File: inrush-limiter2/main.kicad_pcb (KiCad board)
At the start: 2 copper layers, 33 parts, among them K1 RELAY_2RT, P1 CONN_01X04, P2 CONN_01X02, Q1 2N3904, Q2 PN2222A, T1 MY-TRANSFO, U1 LM393, U2 50 ohm NTC

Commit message: good
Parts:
- moved D6 2.54 mm to (148.6, 87.6)
- moved P2 2.54 mm to (143.5, 92.7)
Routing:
- net Net-(D6-Pad1): track 49.8 -> 47.1 mm
- net Net-(D6-Pad2): track 3.81 -> 5.61 mm
- net GND: track 242.2 -> 243.7 mm
- net +5V: track 120.7 -> 119.2 mm
- added copper zone on B.Cu, net GND
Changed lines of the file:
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@@
     (links 59)
     (no_connects 0)
-    (area 110.105 47.685 234.358001 96.28099)
+    (area 110.105 47.685 234.358001 100.585)
     (thickness 1.6)
     (drawings 0)
-    (tracks 192)
+    (tracks 187)
     (zones 0)
     (modules 33)
@@
   )
   (module LEDs:LED-5MM (layer F.Cu)
-    (at 146.05 87.63 90)
+    (at 148.59 87.63 90)
     (descr "LED 5mm round vertical")
     (tags "LED 5mm round vertical")
@@
   )
   (module Pin_Headers:Pin_Header_Straight_1x02 (layer F.Cu)
-    (at 140.97 92.71 180)
+    (at 143.51 92.71 180)
     (descr "Through hole pin header")
     (tags "pin header")
@@
   (segment (start 142.24202 69.85) (end 142.24254 69.85052) (width 1) (layer B.Cu) (net 1) (status 30))
   (segment (start 138.43 69.84798) (end 138.43254 69.85052) (width 1) (layer B.Cu) (net 1) (status 30))
-  (segment (start 137.16 95.25) (end 139.7 95.25) (width 1) (layer B.Cu) (net 2))
-  (segment (start 140.97 93.98) (end 140.97 92.71) (width 1) (layer B.Cu) (net 2) (status 20))
   (segment (start 139.7 95.25) (end 140.97 93.98) (width 1) (layer B.Cu) (net 2))
+  (segment (start 140.97 93.98) (end 143.51 92.71) (width 1) (layer B.Cu) (net 2) (status 20))
+  (segment (start 139.7 95.25) (end 137.16 95.25) (width 1) (layer B.Cu) (net 2))
   (segment (start 149.85746 69.84948) (end 149.85746 74.92746) (width 1) (layer B.Cu) (net 2) (status 10))
   (segment (start 160.02 50.8) (end 146.05 50.8) (width 1) (layer B.Cu) (net 2))
@@
   (segment (start 185.42 59.69) (end 178.74996 59.69) (width 0.75) (layer B.Cu) (net 11) (status 10))
   (segment (start 178.74996 59.69) (end 177.63998 58.58002) (width 0.75) (layer B.Cu) (net 11) (status 20))
-  (segment (start 146.05 81.28) (end 146.05 85.09) (width 1) (layer B.Cu) (net 12) (status 30))
+  (segment (start 146.05 81.28) (end 147.32 81.28) (width 1) (layer B.Cu) (net 12) (status 10))
+  (segment (start 148.59 82.55) (end 148.59 85.09) (width 1) (layer B.Cu) (net 12) (status 20))
+  (segment (start 147.32 81.28) (end 148.59 82.55) (width 1) (layer B.Cu) (net 12))
   (segment (start 130.81 54.61) (end 130.81 57.15) (width 1) (layer B.Cu) (net 13) (status 10))
   (segment (start 128.27 59.69) (end 127 59.69) (width 1) (layer B.Cu) (net 13) (status 20))
@@
   (segment (start 138.43 59.69306) (end 138.43254 59.69052) (width 1) (layer B.Cu) (net 15) (status 30))
   (segment (start 149.85642 59.69052) (end 149.85746 59.68948) (width 1) (layer B.Cu) (net 15) (status 30))
-  (segment (start 146.05 87.63) (end 143.51 87.63) (width 1) (layer B.Cu) (net 16) (status 400000))
-  (segment (start 143.51 87.63) (end 140.97 85.09) (width 1) (layer B.Cu) (net 16) (status 800000))
-  (segment (start 146.05 87.63) (end 146.05 90.17) (width 1) (layer B.Cu) (net 16) (status 400000))
-  (segment (start 149.86 91.44) (end 185.42 91.44) (width 1) (layer B.Cu) (net 16) (status 10))
-  (segment (start 147.32 91.44) (end 149.86 91.44) (width 1) (layer B.Cu) (net 16))
-  (segment (start 146.05 90.17) (end 147.32 91.44) (width 1) (layer B.Cu) (net 16))
-  (segment (start 140.97 85.09) (end 142.24 85.09) (width 1) (layer B.Cu) (net 16) (status 10))
+  (segment (start 148.59 87.63) (end 147.32 87.63) (width 1) (layer B.Cu) (net 16) (status 10))
+  (segment (start 144.78 85.09) (end 140.97 85.09) (width 1) (layer B.Cu) (net 16) (status 20))
+  (segment (start 147.32 87.63) (end 144.78 85.09) (width 1) (layer B.Cu) (net 16))
+  (segment (start 148.59 87.63) (end 152.4 91.44) (width 1) (layer B.Cu) (net 16) (status 10))
+  (segment (start 152.4 91.44) (end 185.42 91.44) (width 1) (layer B.Cu) (net 16) (status 20))
   (segment (start 185.42 66.04) (end 185.42 71.12) (width 1) (layer B.Cu) (net 17) (status 30))
   (segment (start 185.42 71.12) (end 185.42 76.2) (width 1) (layer B.Cu) (net 17) (status 30))
@@
   (segment (start 119.38 77.47) (end 118.11 77.47) (width 1) (layer B.Cu) (net 21) (status 20))
   (segment (start 120.65 76.2) (end 119.38 77.47) (width 1) (layer B.Cu) (net 21))
-  (segment (start 139.7 81.28) (end 138.43 81.28) (width 1) (layer B.Cu) (net 22))
+  (segment (start 144.78 90.17) (end 148.59 93.98) (width 1) (layer B.Cu) (net 22))
+  (segment (start 137.16 83.82) (end 143.51 90.17) (width 1) (layer B.Cu) (net 22) (status 30))
+  (segment (start 143.51 90.17) (end 144.78 90.17) (width 1) (layer B.Cu) (net 22) (status 10))
+  (segment (start 190.5 93.98) (end 148.59 93.98) (width 1) (layer B.Cu) (net 22))
+  (segment (start 193.04 91.44) (end 190.5 93.98) (width 1) (layer B.Cu) (net 22) (status 10))
+  (segment (start 140.97 81.28) (end 138.43 81.28) (width 1) (layer B.Cu) (net 22))
   (segment (start 142.24 73.66) (end 143.51 74.93) (width 1) (layer B.Cu) (net 22))
   (segment (start 143.51 74.93) (end 143.51 78.74) (width 1) (layer B.Cu) (net 22))
   (segment (start 143.51 78.74) (end 140.97 81.28) (width 1) (layer B.Cu) (net 22))
-  (segment (start 140.97 81.28) (end 139.7 81.28) (width 1) (layer B.Cu) (net 22))
-  (segment (start 137.16 82.55) (end 137.16 83.82) (width 1) (layer B.Cu) (net 22) (status 800000))
+  (segment (start 137.16 82.55) (end 137.16 83.82) (width 1) (layer B.Cu) (net 22) (status 20))
   (segment (start 138.43 81.28) (end 137.16 82.55) (width 1) (layer B.Cu) (net 22))
-  (segment (start 146.05 93.98) (end 144.78 92.71) (width 1) (layer B.Cu) (net 22))
-  (segment (start 142.24 90.17) (end 143.51 91.44) (width 1) (layer B.Cu) (net 22))
-  (segment (start 143.51 91.44) (end 144.78 92.71) (width 1) (layer B.Cu) (net 22))
-  (segment (start 142.24 90.17) (end 140.97 90.17) (width 1) (layer B.Cu) (net 22) (status 10))
-  (segment (start 190.5 93.98) (end 146.05 93.98) (width 1) (layer B.Cu) (net 22))
-  (segment (start 193.04 91.44) (end 190.5 93.98) (width 1) (layer B.Cu) (net 22) (status 10))
-  (segment (start 140.97 90.17) (end 139.7 88.9) (width 1) (layer B.Cu) (net 22) (status 10))
-  (segment (start 139.7 86.36) (end 137.16 83.82) (width 1) (layer B.Cu) (net 22) (status 20))
-  (segment (start 139.7 86.36) (end 139.7 88.9) (width 1) (layer B.Cu) (net 22))
   (segment (start 146.05 73.66) (end 142.24 73.66) (width 1) (layer B.Cu) (net 22) (status 10))
   (segment (start 138.43 73.66) (end 142.24 73.66) (width 1) (layer B.Cu) (net 22) (status 10))
@@
   (segment (start 137.16 78.74) (end 139.7 78.74) (width 1) (layer B.Cu) (net 24) (status 10))
   (segment (start 139.7 78.74) (end 140.97 77.47) (width 1) (layer B.Cu) (net 24) (status 20))
+  (zone (net 2) (net_name GND) (layer B.Cu) (hatch edge 0.508)
+    (connect_pads (clearance 0.508))
+    (min_thickness 0.254)
+    (fill yes (arc_segments 16) (thermal_gap 0.508) (thermal_bridge_width 0.508))
+    (polygon
+      (pts
+        (xy 167.64 95.25) (xy 114.3 95.25) (xy 114.3 50.8) (xy 167.64 50.8) (xy 167.64 95.25)
+      )
+    )
+  )
 )

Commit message: more tidying
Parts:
- moved D6 4.02 mm to (149.9, 91.4)
- moved P2 1.80 mm to (142.2, 91.4)
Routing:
- net Net-(D6-Pad2): track 5.61 -> 9.54 mm
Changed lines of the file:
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@@
     (links 59)
     (no_connects 0)
-    (area 110.105 47.685 234.358001 100.585)
+    (area 110.105 47.685 234.358001 99.315)
     (thickness 1.6)
     (drawings 0)
-    (tracks 187)
+    (tracks 188)
     (zones 0)
     (modules 33)
@@
   )
   (module LEDs:LED-5MM (layer F.Cu)
-    (at 148.59 87.63 90)
+    (at 149.86 91.44 90)
     (descr "LED 5mm round vertical")
     (tags "LED 5mm round vertical")
@@
   )
   (module Pin_Headers:Pin_Header_Straight_1x02 (layer F.Cu)
-    (at 143.51 92.71 180)
+    (at 142.24 91.44 180)
     (descr "Through hole pin header")
     (tags "pin header")
@@
   (segment (start 138.43 69.84798) (end 138.43254 69.85052) (width 1) (layer B.Cu) (net 1) (status 30))
   (segment (start 139.7 95.25) (end 140.97 93.98) (width 1) (layer B.Cu) (net 2))
-  (segment (start 140.97 93.98) (end 143.51 92.71) (width 1) (layer B.Cu) (net 2) (status 20))
+  (segment (start 140.97 93.98) (end 142.24 91.44) (width 1) (layer B.Cu) (net 2) (status 20))
   (segment (start 139.7 95.25) (end 137.16 95.25) (width 1) (layer B.Cu) (net 2))
   (segment (start 149.85746 69.84948) (end 149.85746 74.92746) (width 1) (layer B.Cu) (net 2) (status 10))
@@
   (segment (start 178.74996 59.69) (end 177.63998 58.58002) (width 0.75) (layer B.Cu) (net 11) (status 20))
   (segment (start 146.05 81.28) (end 147.32 81.28) (width 1) (layer B.Cu) (net 12) (status 10))
-  (segment (start 148.59 82.55) (end 148.59 85.09) (width 1) (layer B.Cu) (net 12) (status 20))
+  (segment (start 148.59 82.55) (end 149.86 88.9) (width 1) (layer B.Cu) (net 12) (status 20))
   (segment (start 147.32 81.28) (end 148.59 82.55) (width 1) (layer B.Cu) (net 12))
   (segment (start 130.81 54.61) (end 130.81 57.15) (width 1) (layer B.Cu) (net 13) (status 10))
@@
   (segment (start 138.43 59.69306) (end 138.43254 59.69052) (width 1) (layer B.Cu) (net 15) (status 30))
   (segment (start 149.85642 59.69052) (end 149.85746 59.68948) (width 1) (layer B.Cu) (net 15) (status 30))
-  (segment (start 148.59 87.63) (end 147.32 87.63) (width 1) (layer B.Cu) (net 16) (status 10))
-  (segment (start 144.78 85.09) (end 140.97 85.09) (width 1) (layer B.Cu) (net 16) (status 20))
-  (segment (start 147.32 87.63) (end 144.78 85.09) (width 1) (layer B.Cu) (net 16))
-  (segment (start 148.59 87.63) (end 152.4 91.44) (width 1) (layer B.Cu) (net 16) (status 10))
-  (segment (start 152.4 91.44) (end 185.42 91.44) (width 1) (layer B.Cu) (net 16) (status 20))
+  (segment (start 143.51 85.09) (end 140.97 85.09) (width 1) (layer B.Cu) (net 16))
+  (segment (start 149.86 91.44) (end 143.51 85.09) (width 1) (layer B.Cu) (net 16))
+  (segment (start 149.86 91.44) (end 149.86 91.44) (width 1) (layer B.Cu) (net 16) (status 10))
+  (segment (start 149.86 91.44) (end 149.86 91.44) (width 1) (layer B.Cu) (net 16) (status 30))
+  (segment (start 149.86 91.44) (end 185.42 91.44) (width 1) (layer B.Cu) (net 16) (status 10))
   (segment (start 185.42 66.04) (end 185.42 71.12) (width 1) (layer B.Cu) (net 17) (status 30))
   (segment (start 185.42 71.12) (end 185.42 76.2) (width 1) (layer B.Cu) (net 17) (status 30))
@@
   (segment (start 119.38 77.47) (end 118.11 77.47) (width 1) (layer B.Cu) (net 21) (status 20))
   (segment (start 120.65 76.2) (end 119.38 77.47) (width 1) (layer B.Cu) (net 21))
+  (segment (start 144.78 90.17) (end 143.51 88.9) (width 1) (layer B.Cu) (net 22))
+  (segment (start 193.04 91.44) (end 190.5 93.98) (width 1) (layer B.Cu) (net 22) (status 10))
+  (segment (start 190.5 93.98) (end 148.59 93.98) (width 1) (layer B.Cu) (net 22))
   (segment (start 144.78 90.17) (end 148.59 93.98) (width 1) (layer B.Cu) (net 22))
-  (segment (start 137.16 83.82) (end 143.51 90.17) (width 1) (layer B.Cu) (net 22) (status 30))
-  (segment (start 143.51 90.17) (end 144.78 90.17) (width 1) (layer B.Cu) (net 22) (status 10))
-  (segment (start 190.5 93.98) (end 148.59 93.98) (width 1) (layer B.Cu) (net 22))
-  (segment (start 193.04 91.44) (end 190.5 93.98) (width 1) (layer B.Cu) (net 22) (status 10))
+  (segment (start 143.51 88.9) (end 142.24 88.9) (width 1) (layer B.Cu) (net 22) (status 800000))
+  (segment (start 137.16 83.82) (end 142.24 88.9) (width 1) (layer B.Cu) (net 22) (status 20))
   (segment (start 140.97 81.28) (end 138.43 81.28) (width 1) (layer B.Cu) (net 22))
   (segment (start 142.24 73.66) (end 143.51 74.93) (width 1) (layer B.Cu) (net 22))
@@
     (polygon
       (pts
-        (xy 167.64 95.25) (xy 114.3 95.25) (xy 114.3 50.8) (xy 167.64 50.8) (xy 167.64 95.25)
+        (xy 161.29 95.25) (xy 114.3 95.25) (xy 114.3 50.8) (xy 161.29 50.8) (xy 161.29 95.25)
       )
     )

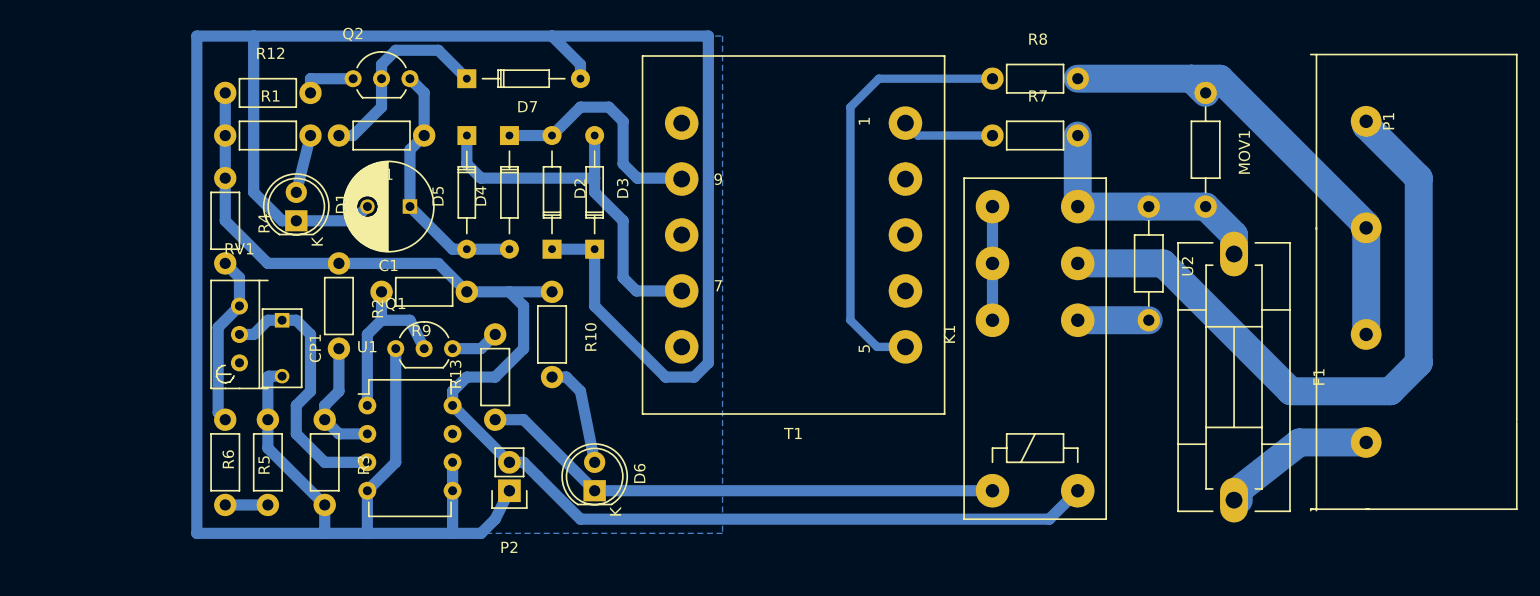
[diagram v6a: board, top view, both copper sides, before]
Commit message: fix capacitor and tidying
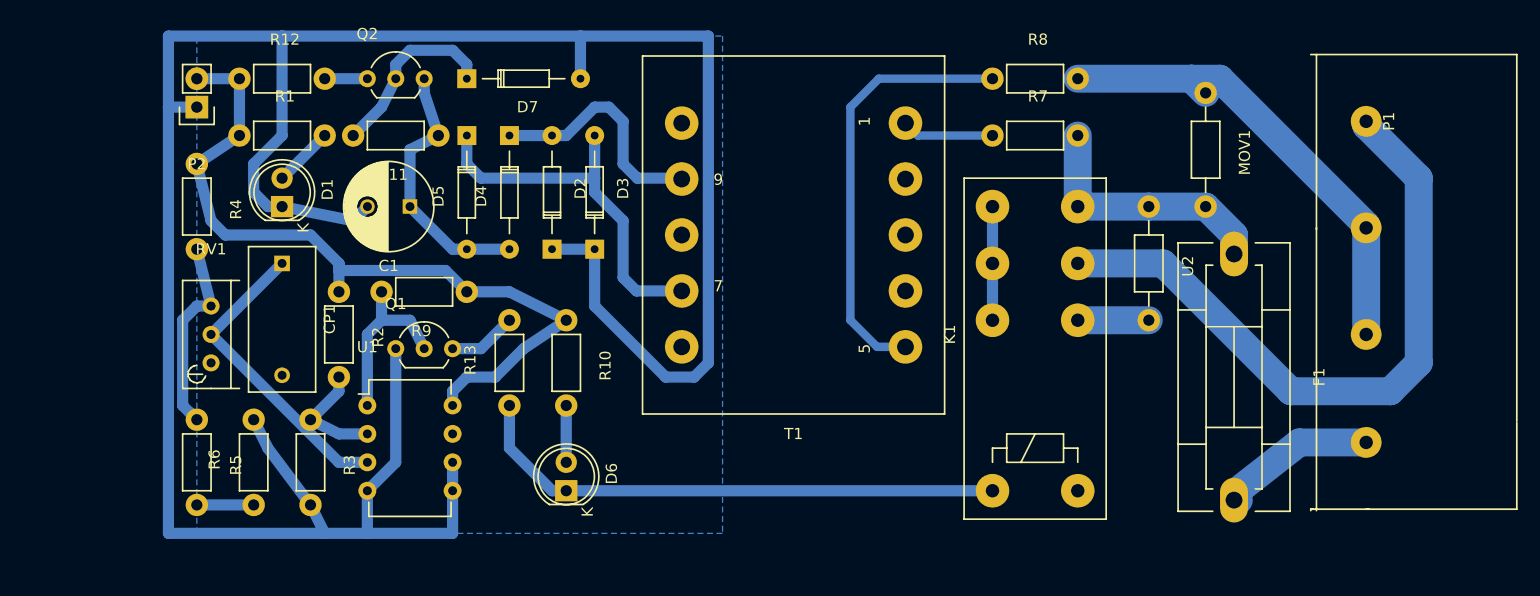
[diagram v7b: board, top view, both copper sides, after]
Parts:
- CP1: footprint Capacitors_ThroughHole:C_Rect_L7_W3.5_P5 -> Capacitors_ThroughHole:C_Rect_L13_W6_H12_P10
- moved P2 44.2 mm to (114.3, 57.1)
- moved CP1 5.08 mm to (121.9, 71.1)
- moved R4 2.84 mm to (114.3, 62.2)
- moved R10 2.84 mm to (147.3, 76.2)
- moved D6 2.54 mm to (147.3, 91.4)
- moved R5 2.54 mm to (114.3, 85.1)
- moved RV1 2.54 mm to (115.6, 80.0)
- moved R2 2.54 mm to (127.0, 73.7)
- moved R13 1.80 mm to (142.2, 83.8)
- moved R12 1.80 mm to (118.1, 54.6)
- moved D1 1.80 mm to (121.9, 66.0)
- moved R3 1.27 mm to (124.5, 85.1)
- moved R6 1.27 mm to (119.4, 92.7)
- moved R1 1.27 mm to (118.1, 59.7)
- moved Q2 1.27 mm to (129.5, 54.6)
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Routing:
- net +5V: track 119.2 -> 70.4 mm
- net GND: track 243.7 -> 238.3 mm
- net Net-(D6-Pad2): track 9.54 -> 5.08 mm
- net Net-(CP1-Pad1): track 24.2 -> 27.7 mm
- net Net-(R4-Pad2): track 15.5 -> 18.6 mm
- net Net-(Q1-Pad3): track 4.34 -> 6.13 mm
- net Net-(D7-Pad1): track 17.9 -> 16.4 mm
- net Net-(D6-Pad1): track 47.1 -> 48.6 mm
- net Net-(Q2-Pad1): track 5.08 -> 3.81 mm
- net Net-(R5-Pad2): track 3.81 -> 5.08 mm
- net Net-(R2-Pad2): track 11.2 -> 10.2 mm
- net Net-(C1-Pad1): track 23.0 -> 23.7 mm

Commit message: update
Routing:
- net +5V: track 70.4 -> 130.3 mm
- net GND: track 238.3 -> 254.0 mm
- net Net-(CP1-Pad1): track 27.7 -> 37.2 mm
- net Net-(D2-Pad2): track 21.4 -> 22.2 mm
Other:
- net class high-voltage: trace_width 0.75 -> 1
